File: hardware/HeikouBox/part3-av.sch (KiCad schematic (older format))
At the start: 92 parts, among them J301 DB15_Female_HighDensity_Mount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, J302 AudioJack3_SwitchTR, Q301 MMBT3904, Q302 MMBT3904, Q303 MMBT3904, Q304 MMBT3904, Q305 MMBT3904, Q306 MMBT3904, Q307 MMBT3904

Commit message: I'm da giant cap that takes all of the space (smaller caps)
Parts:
- C301, C302: footprint Capacitor_SMD:C_1206_3216Metric_Pad1.33x1.80mm_HandSolder -> Capacitor_SMD:C_0805_2012Metric_Pad1.18x1.45mm_HandSolder; symbol Device:CP1 -> Device:C
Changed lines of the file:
@@
 $Descr A4 11693 8268
 encoding utf-8
-Sheet 3 6
+Sheet 2 6
 Title "HeikouBox Mainboard - Audio Video Interface"
 Date "2022-11-11"
@@
 	1400 1200 1400 1250
 $Comp
-L Device:CP1 C?
+L Device:C C?
 U 1 1 62CE6848
 P 5500 3750
@@
 F 0 "C301" H 5600 3800 50  0000 L CNN
 F 1 "10u" H 5600 3700 50  0000 L CNN
-F 2 "Capacitor_SMD:C_1206_3216Metric_Pad1.33x1.80mm_HandSolder" H 5538 3600 50  0001 C CNN
+F 2 "Capacitor_SMD:C_0805_2012Metric_Pad1.18x1.45mm_HandSolder" H 5538 3600 50  0001 C CNN
 F 3 "~" H 5500 3750 50  0001 C CNN
 	1    5500 3750
@@
 	0    -1   -1   0
 $EndComp
-$Comp
-L Device:R R?
-U 1 1 63510156
-P 9950 4500
-AR Path="/63510156" Ref="R?"  Part="1"
-AR Path="/62C73AC4/63510156" Ref="R371"  Part="1"
-F 0 "R371" V 10050 4500 50  0000 C CNN
-F 1 "100" V 9950 4500 50  0000 C CNN
-F 2 "Resistor_SMD:R_0603_1608Metric_Pad0.98x0.95mm_HandSolder" V 9880 4500 50  0001 C CNN
-F 3 "~" H 9950 4500 50  0001 C CNN
-	1    9950 4500
-	0    -1   -1   0
-$EndComp
 Connection ~ 9300 5900
 Wire Wire Line
@@
 $EndComp
 $Comp
-L Device:CP1 C?
+L Device:C C?
 U 1 1 682AA55C
 P 10400 4450
@@
 F 0 "C302" H 10500 4500 50  0000 L CNN
 F 1 "10u" H 10500 4400 50  0000 L CNN
-F 2 "Capacitor_SMD:C_1206_3216Metric_Pad1.33x1.80mm_HandSolder" H 10438 4300 50  0001 C CNN
+F 2 "Capacitor_SMD:C_0805_2012Metric_Pad1.18x1.45mm_HandSolder" H 10438 4300 50  0001 C CNN
 F 3 "~" H 10400 4450 50  0001 C CNN
 	1    10400 4450
@@
 Wire Bus Line
 	850  2000 3400 2000
+$Comp
+L Device:R R?
+U 1 1 63510156
+P 9950 4500
+AR Path="/63510156" Ref="R?"  Part="1"
+AR Path="/62C73AC4/63510156" Ref="R371"  Part="1"
+F 0 "R371" V 10050 4500 50  0000 C CNN
+F 1 "100" V 9950 4500 50  0000 C CNN
+F 2 "Resistor_SMD:R_0603_1608Metric_Pad0.98x0.95mm_HandSolder" V 9880 4500 50  0001 C CNN
+F 3 "~" H 9950 4500 50  0001 C CNN
+	1    9950 4500
+	0    -1   -1   0
+$EndComp
 $EndSCHEMATC

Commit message: BOM reduction
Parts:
- added R373, R374: 2K2, Resistor_SMD:R_0603_1608Metric_Pad0.98x0.95mm_HandSolder, symbol Device:R
- C301, C302: value 10u -> 1u
- C303, C304: value 4n7 -> 10n
- R313, R314: value 2K2 -> 1K
- R317, R318: value 4K7 -> 2K2
- R371, R372: value 100 -> 75R
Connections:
- net 3V3: now also R373.1, R374.1; no longer R317.1, R318.1
- new net: R318.1, R374.2
- new net: R317.1, R373.2
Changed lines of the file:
@@
 AR Path="/62C73AC4/62CE6848" Ref="C301"  Part="1"
 F 0 "C301" H 5600 3800 50  0000 L CNN
-F 1 "10u" H 5600 3700 50  0000 L CNN
+F 1 "1u" H 5600 3700 50  0000 L CNN
 F 2 "Capacitor_SMD:C_0805_2012Metric_Pad1.18x1.45mm_HandSolder" H 5538 3600 50  0001 C CNN
 F 3 "~" H 5500 3750 50  0001 C CNN
@@
 Wire Wire Line
 	9000 4700 9000 4800
-Connection ~ 9300 3800
-Connection ~ 9300 5200
 Text Notes 10500 4300 0    50   ~ 0
 Bulk capacitor\nfor audio buffers
@@
 Wire Wire Line
 	8100 4900 8100 4800
-Wire Wire Line
-	9300 5100 9300 5200
-Wire Wire Line
-	9300 3700 9300 3800
 Connection ~ 10200 5700
 Wire Wire Line
@@
 AR Path="/62C73AC4/63520CD7" Ref="R372"  Part="1"
 F 0 "R372" V 10050 5900 50  0000 C CNN
-F 1 "100" V 9950 5900 50  0000 C CNN
+F 1 "75R" V 9950 5900 50  0000 C CNN
 F 2 "Resistor_SMD:R_0603_1608Metric_Pad0.98x0.95mm_HandSolder" V 9880 5900 50  0001 C CNN
 F 3 "~" H 9950 5900 50  0001 C CNN
@@
 AR Path="/62C73AC4/62F010C1" Ref="R314"  Part="1"
 F 0 "R314" V 8050 5600 50  0000 C CNN
-F 1 "2K2" V 7950 5600 50  0000 C CNN
+F 1 "1K" V 7950 5600 50  0000 C CNN
 F 2 "Resistor_SMD:R_0603_1608Metric_Pad0.98x0.95mm_HandSolder" V 7880 5600 50  0001 C CNN
 F 3 "~" H 7950 5600 50  0001 C CNN
@@
 AR Path="/62C73AC4/62F01012" Ref="C304"  Part="1"
 F 0 "C304" H 8200 6000 50  0000 L CNN
-F 1 "4n7" H 8200 5900 50  0000 L CNN
+F 1 "10n" H 8200 5900 50  0000 L CNN
 F 2 "Capacitor_SMD:C_0603_1608Metric_Pad1.08x0.95mm_HandSolder" H 8138 5800 50  0001 C CNN
 F 3 "~" H 8100 5950 50  0001 C CNN
@@
 AR Path="/62C73AC4/60742614" Ref="R313"  Part="1"
 F 0 "R313" V 8050 4200 50  0000 C CNN
-F 1 "2K2" V 7950 4200 50  0000 C CNN
+F 1 "1K" V 7950 4200 50  0000 C CNN
 F 2 "Resistor_SMD:R_0603_1608Metric_Pad0.98x0.95mm_HandSolder" V 7880 4200 50  0001 C CNN
 F 3 "~" H 7950 4200 50  0001 C CNN
@@
 AR Path="/62C73AC4/607425FC" Ref="C303"  Part="1"
 F 0 "C303" H 8200 4600 50  0000 L CNN
-F 1 "4n7" H 8200 4500 50  0000 L CNN
+F 1 "10n" H 8200 4500 50  0000 L CNN
 F 2 "Capacitor_SMD:C_0603_1608Metric_Pad1.08x0.95mm_HandSolder" H 8138 4400 50  0001 C CNN
 F 3 "~" H 8100 4550 50  0001 C CNN
@@
 AR Path="/62C73AC4/682AA55C" Ref="C302"  Part="1"
 F 0 "C302" H 10500 4500 50  0000 L CNN
-F 1 "10u" H 10500 4400 50  0000 L CNN
+F 1 "1u" H 10500 4400 50  0000 L CNN
 F 2 "Capacitor_SMD:C_0805_2012Metric_Pad1.18x1.45mm_HandSolder" H 10438 4300 50  0001 C CNN
 F 3 "~" H 10400 4450 50  0001 C CNN
@@
 AR Path="/62C73AC4/6074262B" Ref="R317"  Part="1"
 F 0 "R317" H 9050 3950 50  0000 L CNN
-F 1 "4K7" V 9000 3950 50  0000 C CNN
+F 1 "2K2" V 9000 3950 50  0000 C CNN
 F 2 "Resistor_SMD:R_0603_1608Metric_Pad0.98x0.95mm_HandSolder" V 8930 3950 50  0001 C CNN
 F 3 "~" H 9000 3950 50  0001 C CNN
@@
 Wire Wire Line
 	9000 4100 9000 4200
-Wire Wire Line
-	9300 3800 9000 3800
-Wire Wire Line
-	9300 3800 9300 4000
 $Comp
 L Device:C C?
@@
 AR Path="/62C73AC4/6068566E" Ref="R318"  Part="1"
 F 0 "R318" H 9050 5350 50  0000 L CNN
-F 1 "4K7" V 9000 5350 50  0000 C CNN
+F 1 "2K2" V 9000 5350 50  0000 C CNN
 F 2 "Resistor_SMD:R_0603_1608Metric_Pad0.98x0.95mm_HandSolder" V 8930 5350 50  0001 C CNN
 F 3 "~" H 9000 5350 50  0001 C CNN
@@
 	1    0    0    -1
 $EndComp
-Wire Wire Line
-	9300 5200 9000 5200
-Wire Wire Line
-	9300 5200 9300 5400
 Wire Wire Line
 	9000 5500 9000 5600
@@
 Text Label 7400 1400 1    40   ~ 8
 3V3
-Text Label 9300 5100 1    40   ~ 8
+Text Label 9300 5000 1    40   ~ 8
 3V3
-Text Label 9300 3700 1    40   ~ 8
+Text Label 9300 3600 1    40   ~ 8
 3V3
 Text Label 10400 4200 1    40   ~ 8
 3V3
+$Comp
+L Device:R R?
+U 1 1 63510156
+P 9950 4500
+AR Path="/63510156" Ref="R?"  Part="1"
+AR Path="/62C73AC4/63510156" Ref="R371"  Part="1"
+F 0 "R371" V 10050 4500 50  0000 C CNN
+F 1 "75R" V 9950 4500 50  0000 C CNN
+F 2 "Resistor_SMD:R_0603_1608Metric_Pad0.98x0.95mm_HandSolder" V 9880 4500 50  0001 C CNN
+F 3 "~" H 9950 4500 50  0001 C CNN
+	1    9950 4500
+	0    -1   -1   0
+$EndComp
+Wire Wire Line
+	9000 3700 9000 3800
+Wire Wire Line
+	9300 3600 9300 3700
+Wire Wire Line
+	9300 5000 9300 5100
+Wire Wire Line
+	9000 5200 9000 5100
+$Comp
+L Device:R R?
+U 1 1 63BAD55E
+P 9150 3700
+AR Path="/63BAD55E" Ref="R?"  Part="1"
+AR Path="/62C73AC4/63BAD55E" Ref="R373"  Part="1"
+F 0 "R373" V 9250 3700 50  0000 C CNN
+F 1 "2K2" V 9150 3700 50  0000 C CNN
+F 2 "Resistor_SMD:R_0603_1608Metric_Pad0.98x0.95mm_HandSolder" V 9080 3700 50  0001 C CNN
+F 3 "~" H 9150 3700 50  0001 C CNN
+	1    9150 3700
+	0    1    1    0
+$EndComp
+Connection ~ 9300 3700
+Wire Wire Line
+	9300 3700 9300 4000
+$Comp
+L Device:R R?
+U 1 1 63BD7D39
+P 9150 5100
+AR Path="/63BD7D39" Ref="R?"  Part="1"
+AR Path="/62C73AC4/63BD7D39" Ref="R374"  Part="1"
+F 0 "R374" V 9250 5100 50  0000 C CNN
+F 1 "2K2" V 9150 5100 50  0000 C CNN
+F 2 "Resistor_SMD:R_0603_1608Metric_Pad0.98x0.95mm_HandSolder" V 9080 5100 50  0001 C CNN
+F 3 "~" H 9150 5100 50  0001 C CNN
+	1    9150 5100
+	0    1    1    0
+$EndComp
+Connection ~ 9300 5100
+Wire Wire Line
+	9300 5100 9300 5400
 Wire Bus Line
 	850  3400 2900 3400
@@
 Wire Bus Line
 	850  2000 3400 2000
-$Comp
-L Device:R R?
-U 1 1 63510156
-P 9950 4500
-AR Path="/63510156" Ref="R?"  Part="1"
-AR Path="/62C73AC4/63510156" Ref="R371"  Part="1"
-F 0 "R371" V 10050 4500 50  0000 C CNN
-F 1 "100" V 9950 4500 50  0000 C CNN
-F 2 "Resistor_SMD:R_0603_1608Metric_Pad0.98x0.95mm_HandSolder" V 9880 4500 50  0001 C CNN
-F 3 "~" H 9950 4500 50  0001 C CNN
-	1    9950 4500
-	0    -1   -1   0
-$EndComp
 $EndSCHEMATC

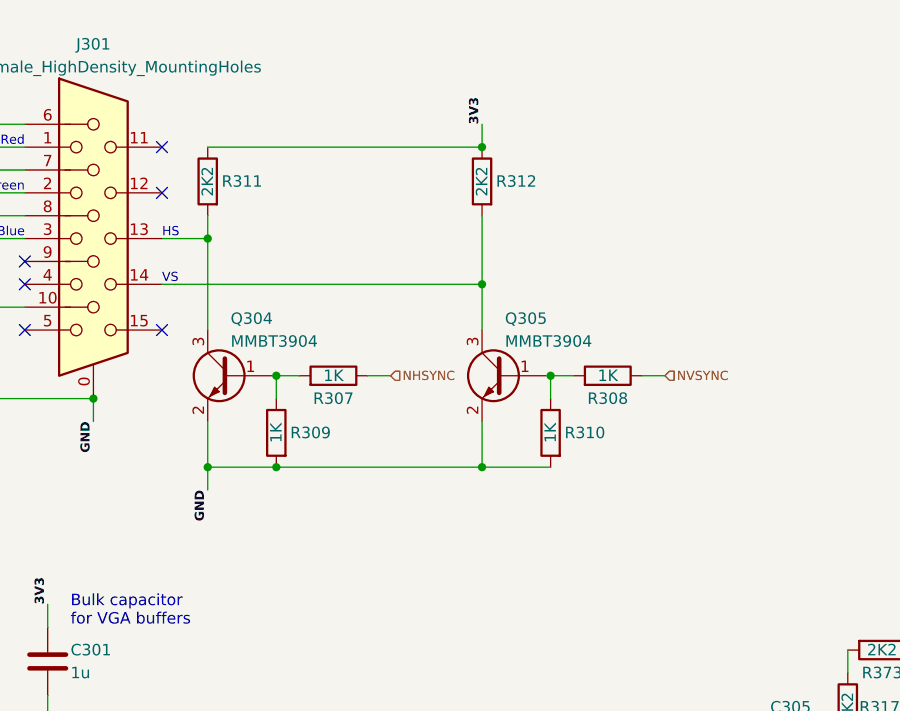
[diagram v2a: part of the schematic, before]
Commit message: Add VGA sync invert jumpers
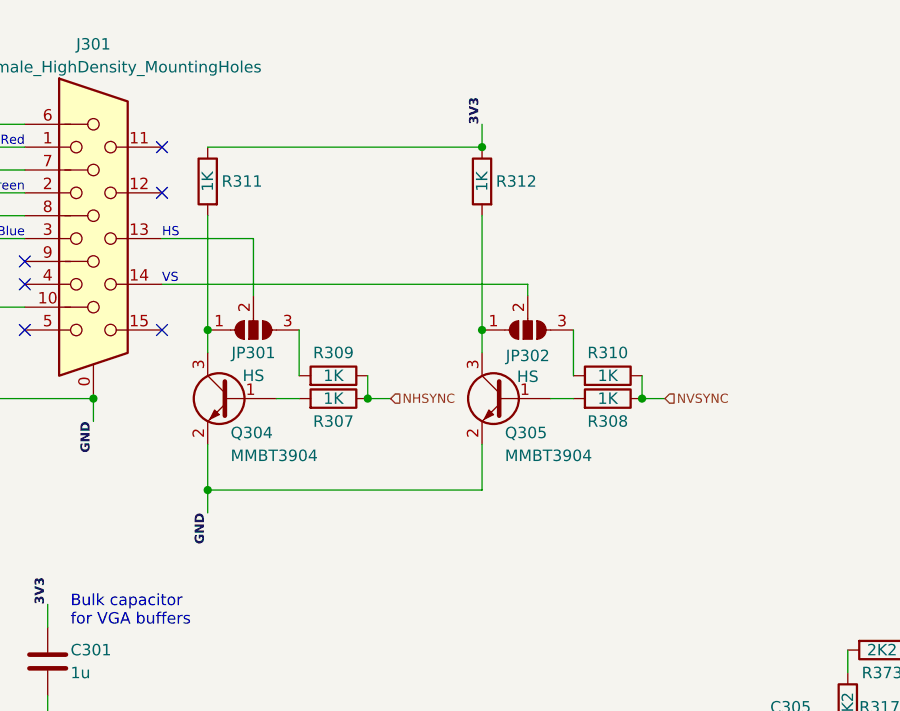
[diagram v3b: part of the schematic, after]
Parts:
- added JP301, JP302: HS, Jumper:SolderJumper-3_P1.3mm_Open_RoundedPad1.0x1.5mm, symbol Jumper:SolderJumper_3_Open
- R311, R312: value 2K2 -> 1K
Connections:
- net GND: no longer R309.2, R310.2
- net NHSYNC: now also R309.1
- net NVSYNC: now also R310.1
- net at Q305.3 (C), R312.2: now also JP302.1 (A); no longer J301.14
- net at Q304.1 (B), R307.2: no longer R309.1
- net at Q305.1 (B), R308.2: no longer R310.1
- net at Q304.3 (C), R311.2: now also JP301.1 (A); no longer J301.13
- new net: JP301.3 (B), R309.2
- new net: JP302.3 (B), R310.2
- new net: J301.13, JP301.2 (C)
- new net: J301.14, JP302.2 (C)
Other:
- moved on the sheet: Q304, Q305, R307, R308, R309, R310
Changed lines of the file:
@@
 AR Path="/62C73AC4/6081298B" Ref="R312"  Part="1"
 F 0 "R312" H 7250 1650 50  0000 C CNN
-F 1 "2K2" V 7400 1650 50  0000 C CNN
+F 1 "1K" V 7400 1650 50  0000 C CNN
 F 2 "Resistor_SMD:R_0603_1608Metric_Pad0.98x0.95mm_HandSolder" V 7330 1650 50  0001 C CNN
 F 3 "~" H 7400 1650 50  0001 C CNN
@@
 	6200 1500 7400 1500
 Wire Wire Line
-	6500 2500 6600 2500
-Wire Wire Line
-	7700 2500 7800 2500
-Wire Wire Line
-	6000 1900 6200 1900
-$Comp
-L Device:R R?
-U 1 1 6086A55B
-P 6500 2750
-AR Path="/6086A55B" Ref="R?"  Part="1"
-AR Path="/62C73AC4/6086A55B" Ref="R309"  Part="1"
-F 0 "R309" H 6350 2750 50  0000 C CNN
-F 1 "1K" V 6500 2750 50  0000 C CNN
-F 2 "Resistor_SMD:R_0603_1608Metric_Pad0.98x0.95mm_HandSolder" V 6430 2750 50  0001 C CNN
-F 3 "~" H 6500 2750 50  0001 C CNN
-	1    6500 2750
-	-1   0    0    -1
-$EndComp
+	6500 2600 6600 2600
+Wire Wire Line
+	7700 2600 7800 2600
 $Comp
 L Connector:DB15_Female_HighDensity_MountingHoles J?
@@
 L Device:R R?
 U 1 1 6086A561
-P 6750 2500
+P 6750 2600
 AR Path="/6086A561" Ref="R?"  Part="1"
 AR Path="/62C73AC4/6086A561" Ref="R307"  Part="1"
-F 0 "R307" V 6650 2500 50  0000 C CNN
-F 1 "1K" V 6750 2500 50  0000 C CNN
-F 2 "Resistor_SMD:R_0603_1608Metric_Pad0.98x0.95mm_HandSolder" V 6680 2500 50  0001 C CNN
-F 3 "~" H 6750 2500 50  0001 C CNN
-	1    6750 2500
+F 0 "R307" V 6650 2600 50  0000 C CNN
+F 1 "1K" V 6750 2600 50  0000 C CNN
+F 2 "Resistor_SMD:R_0603_1608Metric_Pad0.98x0.95mm_HandSolder" V 6680 2600 50  0001 C CNN
+F 3 "~" H 6750 2600 50  0001 C CNN
+	1    6750 2600
 	0    1    -1   0
 $EndComp
-Wire Wire Line
-	8200 2500 8100 2500
-Text HLabel 8200 2500 2    40   Input ~ 0
-NVSYNC
 $Comp
 L Transistor_BJT:MMBT3904 Q?
 U 1 1 62CE65EF
-P 6300 2500
+P 6300 2600
 AR Path="/62CE65EF" Ref="Q?"  Part="1"
 AR Path="/62C73AC4/62CE65EF" Ref="Q304"  Part="1"
-F 0 "Q304" H 6300 2750 50  0000 R CNN
-F 1 "MMBT3904" H 6300 2650 50  0000 R CNN
-F 2 "Package_TO_SOT_SMD:SOT-23" H 6500 2425 50  0001 L CIN
-F 3 "https://www.fairchildsemi.com/datasheets/2N/2N3904.pdf" H 6300 2500 50  0001 L CNN
-	1    6300 2500
+F 0 "Q304" H 6300 2450 50  0000 R CNN
+F 1 "MMBT3904" H 6300 2350 50  0000 R CNN
+F 2 "Package_TO_SOT_SMD:SOT-23" H 6500 2525 50  0001 L CIN
+F 3 "https://www.fairchildsemi.com/datasheets/2N/2N3904.pdf" H 6300 2600 50  0001 L CNN
+	1    6300 2600
 	-1   0    0    -1
 $EndComp
-Text HLabel 7000 2500 2    40   Input ~ 0
-NHSYNC
-Wire Wire Line
-	7000 2500 6900 2500
 $Comp
 L Device:R R?
 U 1 1 62CE65B1
-P 7700 2750
+P 7950 2500
 AR Path="/62CE65B1" Ref="R?"  Part="1"
 AR Path="/62C73AC4/62CE65B1" Ref="R310"  Part="1"
-F 0 "R310" H 7550 2750 50  0000 C CNN
-F 1 "1K" V 7700 2750 50  0000 C CNN
-F 2 "Resistor_SMD:R_0603_1608Metric_Pad0.98x0.95mm_HandSolder" V 7630 2750 50  0001 C CNN
-F 3 "~" H 7700 2750 50  0001 C CNN
-	1    7700 2750
-	-1   0    0    -1
-$EndComp
-$Comp
-L Device:R R?
-U 1 1 62CE65B7
-P 7950 2500
-AR Path="/62CE65B7" Ref="R?"  Part="1"
-AR Path="/62C73AC4/62CE65B7" Ref="R308"  Part="1"
-F 0 "R308" V 7850 2500 50  0000 C CNN
+F 0 "R310" V 8050 2500 50  0000 C CNN
 F 1 "1K" V 7950 2500 50  0000 C CNN
 F 2 "Resistor_SMD:R_0603_1608Metric_Pad0.98x0.95mm_HandSolder" V 7880 2500 50  0001 C CNN
 F 3 "~" H 7950 2500 50  0001 C CNN
 	1    7950 2500
+	0    1    -1   0
+$EndComp
+$Comp
+L Device:R R?
+U 1 1 62CE65B7
+P 7950 2600
+AR Path="/62CE65B7" Ref="R?"  Part="1"
+AR Path="/62C73AC4/62CE65B7" Ref="R308"  Part="1"
+F 0 "R308" V 7850 2600 50  0000 C CNN
+F 1 "1K" V 7950 2600 50  0000 C CNN
+F 2 "Resistor_SMD:R_0603_1608Metric_Pad0.98x0.95mm_HandSolder" V 7880 2600 50  0001 C CNN
+F 3 "~" H 7950 2600 50  0001 C CNN
+	1    7950 2600
 	0    1    -1   0
 $EndComp
@@
 L Transistor_BJT:MMBT3904 Q?
 U 1 1 6086A569
-P 7500 2500
+P 7500 2600
 AR Path="/6086A569" Ref="Q?"  Part="1"
 AR Path="/62C73AC4/6086A569" Ref="Q305"  Part="1"
-F 0 "Q305" H 7500 2750 50  0000 R CNN
-F 1 "MMBT3904" H 7500 2650 50  0000 R CNN
-F 2 "Package_TO_SOT_SMD:SOT-23" H 7700 2425 50  0001 L CIN
-F 3 "https://www.fairchildsemi.com/datasheets/2N/2N3904.pdf" H 7500 2500 50  0001 L CNN
-	1    7500 2500
+F 0 "Q305" H 7500 2450 50  0000 R CNN
+F 1 "MMBT3904" H 7500 2350 50  0000 R CNN
+F 2 "Package_TO_SOT_SMD:SOT-23" H 7700 2525 50  0001 L CIN
+F 3 "https://www.fairchildsemi.com/datasheets/2N/2N3904.pdf" H 7500 2600 50  0001 L CNN
+	1    7500 2600
 	-1   0    0    -1
 $EndComp
-Wire Wire Line
-	6200 1900 6200 1800
-Wire Wire Line
-	6000 2100 7400 2100
 Text HLabel 700  5700 0    40   Input ~ 0
 GND
 Wire Wire Line
 	7400 1400 7400 1500
-Wire Wire Line
-	7400 1800 7400 2100
 $Comp
 L Device:R R?
@@
 AR Path="/62C73AC4/6086A577" Ref="R311"  Part="1"
 F 0 "R311" H 6050 1650 50  0000 C CNN
-F 1 "2K2" V 6200 1650 50  0000 C CNN
+F 1 "1K" V 6200 1650 50  0000 C CNN
 F 2 "Resistor_SMD:R_0603_1608Metric_Pad0.98x0.95mm_HandSolder" V 6130 1650 50  0001 C CNN
 F 3 "~" H 6200 1650 50  0001 C CNN
@@
 	5000 1900 5000 4300
 Wire Wire Line
-	6200 2700 6200 2900
-Wire Wire Line
-	6500 2600 6500 2500
-Connection ~ 6500 2500
-Wire Wire Line
-	6500 2900 6200 2900
-Connection ~ 6200 2900
-Wire Wire Line
-	6200 2900 6200 3000
-Wire Wire Line
-	7700 2600 7700 2500
-Wire Wire Line
-	7400 2700 7400 2900
-Connection ~ 7700 2500
-Wire Wire Line
-	7700 2900 7400 2900
-Wire Wire Line
-	6200 2300 6200 1900
-Connection ~ 6200 1900
-Wire Wire Line
-	7400 2100 7400 2300
-Connection ~ 7400 2100
+	6200 2800 6200 3000
+Connection ~ 6200 3000
+Wire Wire Line
+	6200 3000 6200 3100
+Wire Wire Line
+	7400 2800 7400 3000
 Text Notes 5600 3600 0    50   ~ 0
 Bulk capacitor\nfor VGA buffers
@@
 Text Label 3900 4800 3    40   ~ 8
 GND
-Text Label 6200 3000 3    40   ~ 8
+Text Label 6200 3100 3    40   ~ 8
 GND
 Wire Wire Line
@@
 Text Label 5700 2700 3    40   ~ 8
 GND
-Wire Wire Line
-	7400 2900 6500 2900
-Connection ~ 6500 2900
-Connection ~ 7400 2900
 Connection ~ 5700 2600
 Text Label 8100 6300 3    40   ~ 8
@@
 Wire Wire Line
 	9300 5100 9300 5400
+$Comp
+L Jumper:SolderJumper_3_Open JP?
+U 1 1 642F41AE
+P 7600 2300
+AR Path="/646E3FCF/642F41AE" Ref="JP?"  Part="1"
+AR Path="/62C73AC4/642F41AE" Ref="JP302"  Part="1"
+F 0 "JP302" H 7600 2413 50  0000 C CNN
+F 1 "HS" H 7600 2504 50  0000 C CNN
+F 2 "Jumper:SolderJumper-3_P1.3mm_Open_RoundedPad1.0x1.5mm" H 7600 2300 50  0001 C CNN
+F 3 "~" H 7600 2300 50  0001 C CNN
+	1    7600 2300
+	1    0    0    1
+$EndComp
+Wire Wire Line
+	7400 1800 7400 2300
+Wire Wire Line
+	6200 3000 7400 3000
+Wire Wire Line
+	6000 2100 7600 2100
+Wire Wire Line
+	8100 2500 8100 2600
+Connection ~ 8100 2600
+Connection ~ 6900 2600
+Wire Wire Line
+	6200 1800 6200 2300
+Wire Wire Line
+	6400 1900 6000 1900
+Connection ~ 6200 2300
+Wire Wire Line
+	6200 2300 6200 2400
+Wire Wire Line
+	6400 1900 6400 2150
+Wire Wire Line
+	7800 2300 7800 2500
+Connection ~ 7400 2300
+Wire Wire Line
+	7400 2300 7400 2400
+Wire Wire Line
+	7600 2100 7600 2150
+Wire Wire Line
+	6600 2300 6600 2500
+Wire Wire Line
+	6900 2500 6900 2600
+$Comp
+L Device:R R?
+U 1 1 6086A55B
+P 6750 2500
+AR Path="/6086A55B" Ref="R?"  Part="1"
+AR Path="/62C73AC4/6086A55B" Ref="R309"  Part="1"
+F 0 "R309" V 6850 2500 50  0000 C CNN
+F 1 "1K" V 6750 2500 50  0000 C CNN
+F 2 "Resistor_SMD:R_0603_1608Metric_Pad0.98x0.95mm_HandSolder" V 6680 2500 50  0001 C CNN
+F 3 "~" H 6750 2500 50  0001 C CNN
+	1    6750 2500
+	0    1    -1   0
+$EndComp
+$Comp
+L Jumper:SolderJumper_3_Open JP?
+U 1 1 64392E8C
+P 6400 2300
+AR Path="/646E3FCF/64392E8C" Ref="JP?"  Part="1"
+AR Path="/62C73AC4/64392E8C" Ref="JP301"  Part="1"
+F 0 "JP301" H 6400 2400 50  0000 C CNN
+F 1 "HS" H 6400 2500 50  0000 C CNN
+F 2 "Jumper:SolderJumper-3_P1.3mm_Open_RoundedPad1.0x1.5mm" H 6400 2300 50  0001 C CNN
+F 3 "~" H 6400 2300 50  0001 C CNN
+	1    6400 2300
+	1    0    0    1
+$EndComp
+Wire Wire Line
+	8200 2600 8100 2600
+Text HLabel 8200 2600 2    40   Input ~ 0
+NVSYNC
+Wire Bus Line
+	850  2000 3400 2000
 Wire Bus Line
 	850  3400 2900 3400
 Wire Bus Line
 	850  600  2900 600
-Wire Bus Line
-	850  2000 3400 2000
+Wire Wire Line
+	7000 2600 6900 2600
+Text HLabel 7000 2600 2    40   Input ~ 0
+NHSYNC
 $EndSCHEMATC
